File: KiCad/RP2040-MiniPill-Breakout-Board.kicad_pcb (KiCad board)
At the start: 2 copper layers, 56 x 72 mm, 8 parts, among them J1 Conn_01x20_Socket, J2 Conn_01x20_Socket, J3 Screw_Terminal_01x20, J4 Screw_Terminal_01x20

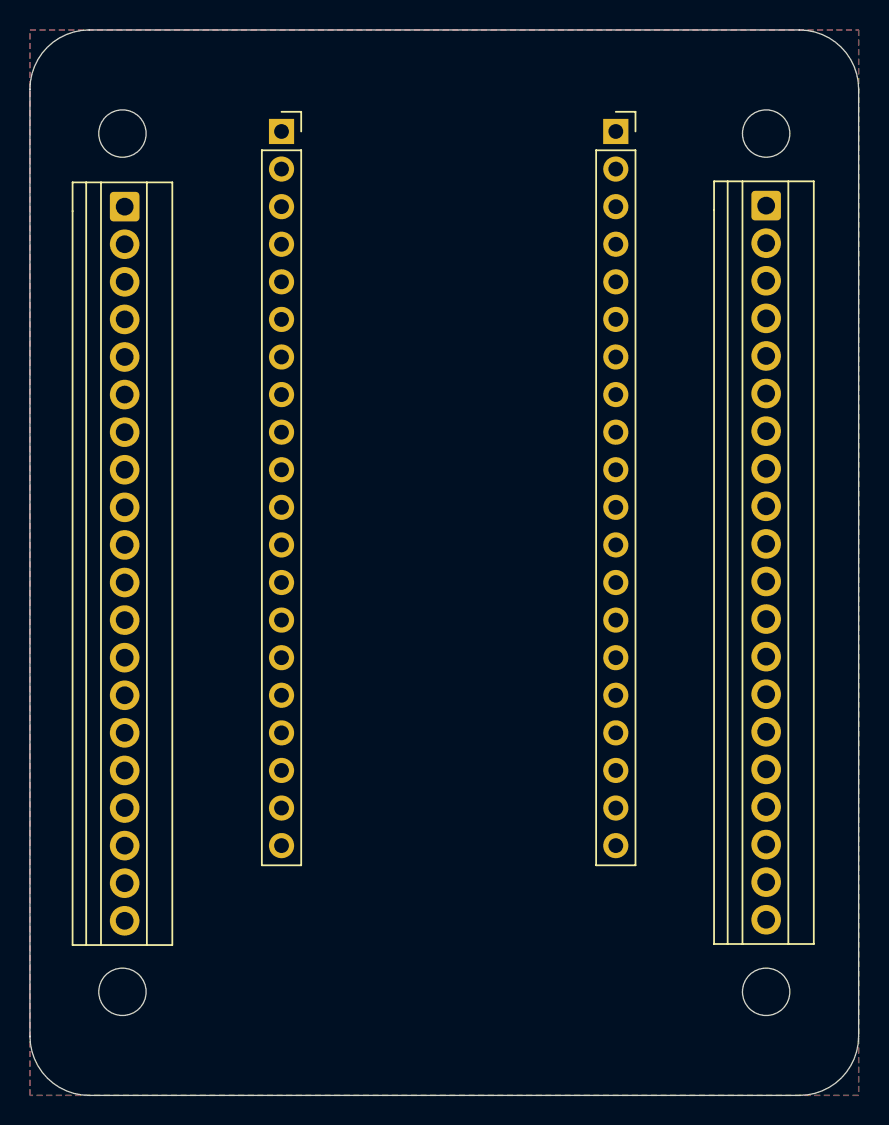
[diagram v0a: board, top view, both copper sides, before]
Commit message: adding Batteryholder
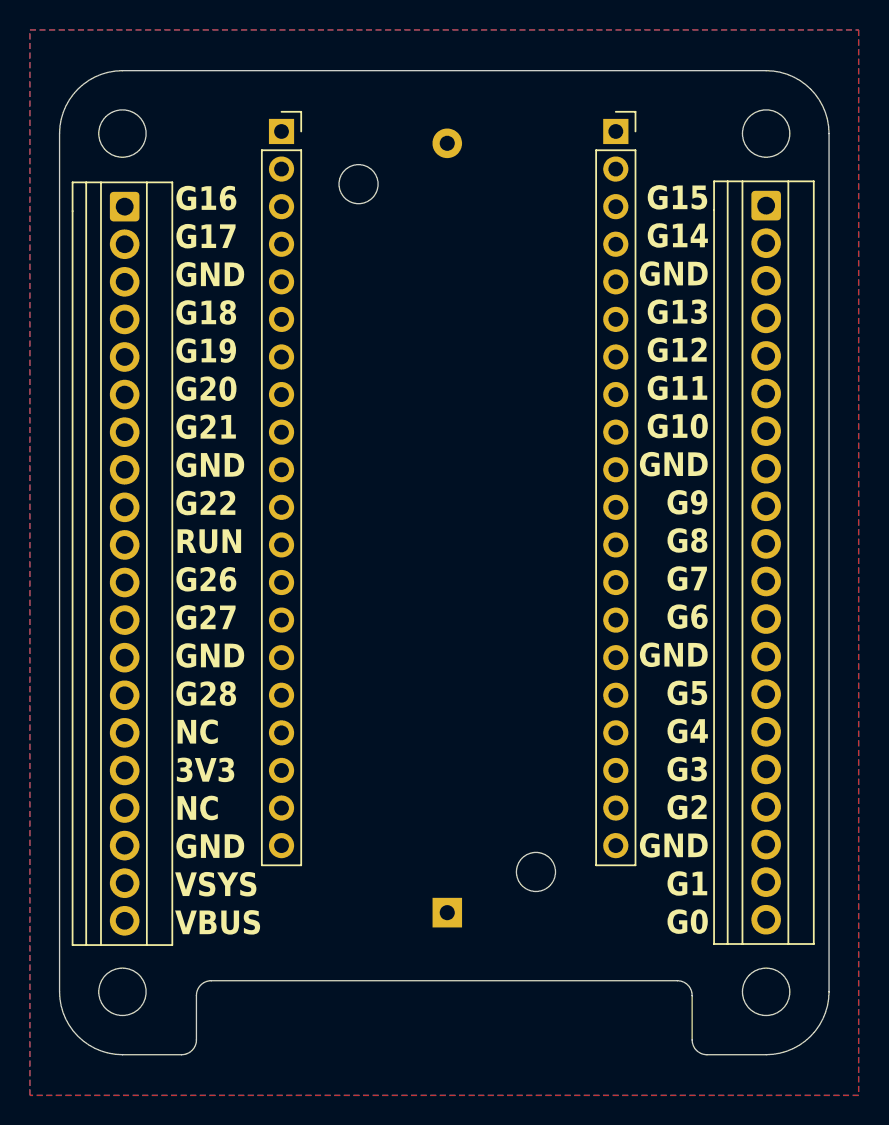
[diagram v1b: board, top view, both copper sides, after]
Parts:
- added BT1: Battery_Cell, Battery:BatteryHolder_Keystone_2460_1xAA, B.Cu at (144.4, 118.3)
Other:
- board size 56 x 72 mm -> 52 x 66.5 mm
- board text added: "G15 G14 GND G13 G12 G11 G10 GND G9 G8 G7 G6 GND G5 G4 G3 G2 GND G1 G0"
- board text added: "G16 G17 GND G18 G19 G20 G21 GND G22 RUN G26 G27 GND G28 NC 3V3 NC GND VSYS VBUS"

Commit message: Making some finetuning of 3dmodels. Adding aimation to README file.
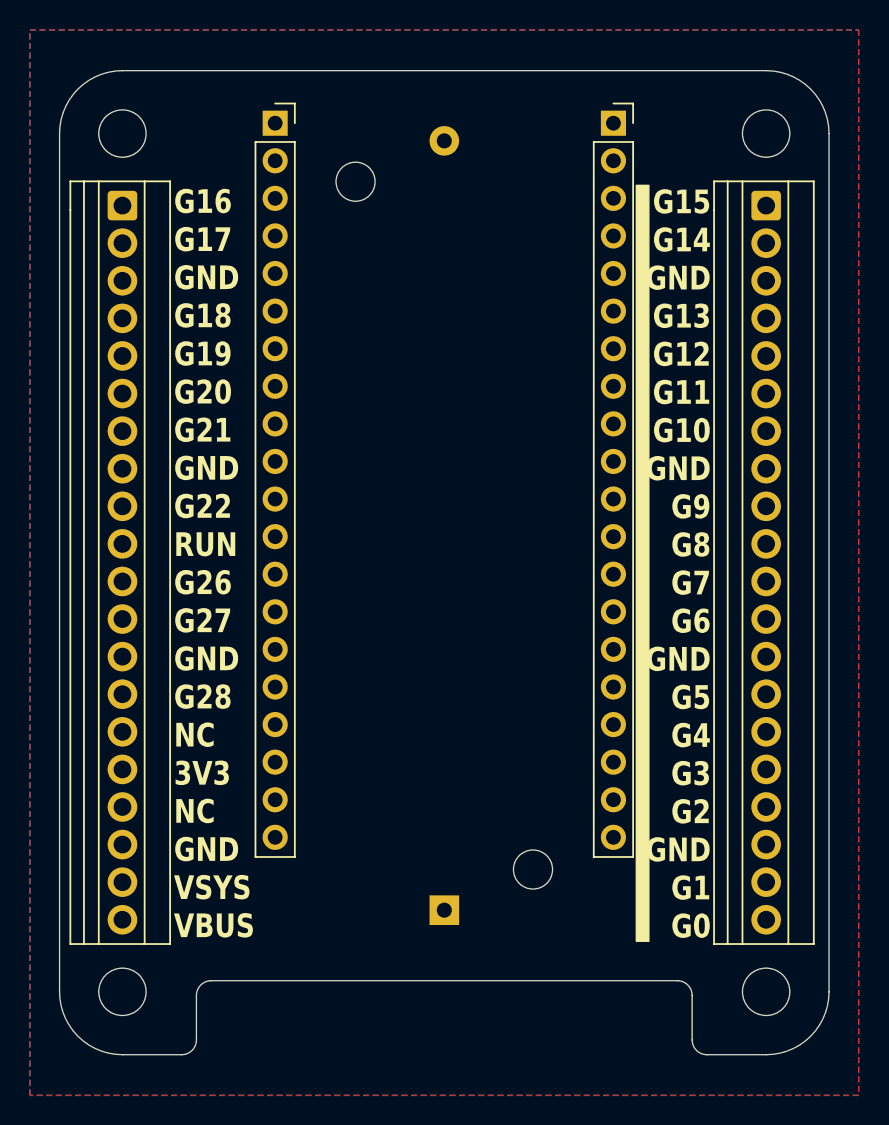
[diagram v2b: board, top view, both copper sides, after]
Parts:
- moved J1 0.71 mm to (132.8, 65.0)
- moved J2 0.58 mm to (155.6, 65.0)
- moved BT1 0.26 mm to (144.2, 118.2)
- moved J3 0.17 mm to (122.5, 70.6)
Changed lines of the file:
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@@
 	(net 82 "unconnected-(BT1---Pad2)")
 	(footprint "TerminalBlock:TerminalBlock_Xinya_XY308-2.54-20P_1x20_P2.54mm_Horizontal"
+		(locked yes)
 		(layer "F.Cu")
-		(at 122.6 70.64 -90)
+		(at 122.45 70.57 -90)
 		(descr "Terminal Block Xinya XY308-2.54-20P, 20 pins, pitch 2.54mm, size 51.3x6.5mm, drill diameter 1.2mm, pad diameter 2mm, http://www.xinyaelectronic.com/product/xy308-254, script-generated using https://gitlab.com/kicad/libraries/kicad-footprint-generator/-/tree/master/scripts/TerminalBlock_Xinya")
 		(tags "THT Terminal Block Xinya XY308-2.54-20P pitch 2.54mm size 51.3x6.5mm drill 1.2mm pad 2mm")
@@
 		(model "${KIPRJMOD}/Libraries/3dmodels/pxc_1725737_09_02_MPT-0-5-10-2-54_3D.stp"
 			(offset
-				(xyz -1.27 -3.175 0)
+				(xyz -1.4478 -3.048 0)
 			)
 			(scale
@@
 		(model "${KIPRJMOD}/Libraries/3dmodels/pxc_1725737_09_02_MPT-0-5-10-2-54_3D.stp"
 			(offset
-				(xyz 24.13 -3.175 0)
+				(xyz 23.9268 -3.048 0)
 			)
 			(scale
@@
 	)
 	(footprint "TerminalBlock:TerminalBlock_Xinya_XY308-2.54-20P_1x20_P2.54mm_Horizontal"
+		(locked yes)
 		(layer "F.Cu")
 		(at 165.95 70.57 -90)
@@
 		)
 		(fp_text user "${REFERENCE}"
-			(at 24.13 2.15 90)
+			(at 0.005 -2.35 0)
 			(layer "F.Fab")
 			(effects
@@
 		(locked yes)
 		(layer "F.Cu")
-		(at 155.79 65.56)
+		(at 155.63 65)
 		(descr "Through hole straight socket strip, 1x20, 2.54mm pitch, single row (from Kicad 4.0.7), script generated")
 		(tags "Through hole socket strip THT 1x20 2.54mm single row")
@@
 		(embedded_fonts no)
 		(model "${KIPRJMOD}/Libraries/3dmodels/5U210010_PC 210010 G 5U.stp"
+			(hide yes)
 			(opacity 0.4300)
 			(offset
@@
 		(locked yes)
 		(layer "F.Cu")
-		(at 133.2 65.56)
+		(at 132.77 65)
 		(descr "Through hole straight socket strip, 1x20, 2.54mm pitch, single row (from Kicad 4.0.7), script generated")
 		(tags "Through hole socket strip THT 1x20 2.54mm single row")
@@
 	)
 	(footprint "Battery:BatteryHolder_Keystone_2460_1xAA"
+		(locked yes)
 		(layer "B.Cu")
-		(at 144.4 118.35 90)
+		(at 144.2 118.185 90)
 		(descr "https://www.keyelco.com/product-pdf.cfm?p=1025")
 		(tags "AA battery cell holder")
@@
 			(at -0.02 9.42 90)
 			(layer "B.SilkS")
+			(hide yes)
 			(effects
 				(font
@@
 			(at 24.5 0 90)
 			(layer "B.Fab")
+			(hide yes)
 			(effects
 				(font
@@
 			)
 		)
-		(model "${KIPRJMOD}/Libraries/3dmodels/2460.STEP"
+		(model "${KIPRJMOD}/Libraries/3dmodels/2460_shorted.STEP"
 			(offset
-				(xyz 23 0.75 10.5)
+				(xyz 23 0.7499999986 10.16980001)
 			)
 			(scale
@@
 		)
 	)
+	(gr_rect
+		(start 157.175 69.2)
+		(end 158.025 120.285)
+		(stroke
+			(width 0.09)
+			(type solid)
+		)
+		(fill yes)
+		(locked yes)
+		(layer "F.SilkS")
+	)
 	(gr_line
 		(start 122.45 61.45)
@@
 	)
 	(gr_text "G16\nG17\nGND\nG18\nG19\nG20\nG21\nGND\nG22\nRUN\nG26\nG27\nGND\nG28\nNC\n3V3\nNC\nGND\nVSYS\nVBUS"
-		(at 126 120 0)
+		(locked yes)
+		(at 125.925 120.2 0)
 		(layer "F.SilkS" knockout)
 		(effects
 			(font
-				(size 1.6 1.4)
-				(thickness 0.25)
+				(size 1.6 1.3)
+				(thickness 0.275)
 				(bold yes)
 			)
@@
 	)
 	(gr_text "G15\nG14\nGND\nG13\nG12\nG11\nG10\nGND\nG9\nG8\nG7\nG6\nGND\nG5\nG4\nG3\nG2\nGND\nG1\nG0"
-		(at 162.1 119.95 0)
+		(locked yes)
+		(at 162.225 120.225 0)
 		(layer "F.SilkS" knockout)
 		(effects
 			(font
-				(size 1.6 1.4)
-				(thickness 0.25)
+				(size 1.6 1.3)
+				(thickness 0.275)
 				(bold yes)
 			)
@@
 			(keep_text_aligned yes)
 		)
-		(gr_text "56"
+		(gr_text "2204.7244"
 			(at 144.2 141.15 0)
 			(layer "Cmts.User")
@@
 		(layer "Cmts.User")
 		(pts
+			(xy 144.2 66.2) (xy 144.2 61.45)
+		)
+		(height -5.5)
+		(orientation 1)
+		(format
+			(prefix "")
+			(suffix "")
+			(units 3)
+			(units_format 0)
+			(precision 4)
+			(suppress_zeroes yes)
+		)
+		(style
+			(thickness 0.1)
+			(arrow_length 1.27)
+			(text_position_mode 0)
+			(arrow_direction outward)
+			(extension_height 0.58642)
+			(extension_offset 0.5)
+			(keep_text_aligned yes)
+		)
+		(gr_text "187.0079"
+			(at 137.55 63.825 90)
+			(layer "Cmts.User")
+			(effects
+				(font
+					(size 1 1)
+					(thickness 0.15)
+				)
+			)
+		)
+	)
+	(dimension
+		(type orthogonal)
+		(layer "Cmts.User")
+		(pts
 			(xy 122.45 65.7) (xy 165.95 65.7)
 		)
@@
 			(keep_text_aligned yes)
 		)
-		(gr_text "43.5"
+		(gr_text "1712.5984"
 			(at 144.2 135.65 0)
 			(layer "Cmts.User")
@@
 			(keep_text_aligned yes)
 		)
-		(gr_text "58"
+		(gr_text "2283.4646"
 			(at 178.05 94.7 90)
 			(layer "Cmts.User")
@@
 			(keep_text_aligned yes)
 		)
-		(gr_text "72"
+		(gr_text "2834.6457"
 			(at 185.15 94.7 90)
 			(layer "Cmts.User")
 			(effects
+				(font
+					(size 1 1)
+					(thickness 0.15)
+				)
+			)
+		)
+	)
+	(dimension
+		(type orthogonal)
+		(layer "Cmts.User")
+		(pts
+			(xy 144.2 118.185) (xy 144.2 122.95)
+		)
+		(height -4.5)
+		(orientation 1)
+		(format
+			(prefix "")
+			(suffix "")
+			(units 3)
+			(units_format 0)
+			(precision 4)
+			(suppress_zeroes yes)
+		)
+		(style
+			(thickness 0.1)
+			(arrow_length 1.27)
+			(text_position_mode 0)
+			(arrow_direction outward)
+			(extension_height 0.58642)
+			(extension_offset 0.5)
+			(keep_text_aligned yes)
+		)
+		(gr_text "187.5984"
+			(at 138.55 120.5675 90)
+			(layer "Cmts.User")
+			(effects
+				(font
+					(size 1 1)
+					(thickness 0.15)
+				)
+			)
+		)
+	)
+	(dimension
+		(type orthogonal)
+		(layer "Cmts.User")
+		(pts
+			(xy 132.77 65) (xy 155.63 65)
+		)
+		(height -9.75)
+		(orientation 0)
+		(format
+			(prefix "")
+			(suffix "")
+			(units 3)
+			(units_format 0)
+			(precision 4)
+			(suppress_zeroes yes)
+		)
+		(style
+			(thickness 0.1)
+			(arrow_length 1.27)
+			(text_position_mode 0)
+			(arrow_direction outward)
+			(extension_height 0.58642)
+			(extension_offset 0.5)
+			(keep_text_aligned yes)
+		)
+		(gr_text "900"
+			(at 144.2 54.1 0)
+			(layer "Cmts.User")
+			(effects

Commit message: adding over and undervoltage monitoring
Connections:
- J1 pad 1: unconnected-(J1-Pin_1-Pad1) -> Net-(J1-Pin_1)
- J1 pad 10: unconnected-(J1-Pin_10-Pad10) -> Net-(J1-Pin_10)
- J1 pad 11: unconnected-(J1-Pin_11-Pad11) -> Net-(J1-Pin_11)
- J1 pad 12: unconnected-(J1-Pin_12-Pad12) -> Net-(J1-Pin_12)
- J1 pad 13: unconnected-(J1-Pin_13-Pad13) -> /GND
- J1 pad 14: unconnected-(J1-Pin_14-Pad14) -> Net-(J1-Pin_14)
- J1 pad 15: unconnected-(J1-Pin_15-Pad15) -> Net-(J1-Pin_15)
- J1 pad 16: unconnected-(J1-Pin_16-Pad16) -> Net-(J1-Pin_16)
- J1 pad 17: unconnected-(J1-Pin_17-Pad17) -> Net-(J1-Pin_17)
- J1 pad 18: unconnected-(J1-Pin_18-Pad18) -> /GND
- J1 pad 19: unconnected-(J1-Pin_19-Pad19) -> Net-(J1-Pin_19)
- J1 pad 2: unconnected-(J1-Pin_2-Pad2) -> Net-(J1-Pin_2)
- J1 pad 20: unconnected-(J1-Pin_20-Pad20) -> Net-(J1-Pin_20)
- J1 pad 3: unconnected-(J1-Pin_3-Pad3) -> /GND
- J1 pad 4: unconnected-(J1-Pin_4-Pad4) -> Net-(J1-Pin_4)
- J1 pad 5: unconnected-(J1-Pin_5-Pad5) -> Net-(J1-Pin_5)
- J1 pad 6: unconnected-(J1-Pin_6-Pad6) -> Net-(J1-Pin_6)
- J1 pad 7: unconnected-(J1-Pin_7-Pad7) -> Net-(J1-Pin_7)
- J1 pad 8: unconnected-(J1-Pin_8-Pad8) -> /GND
- J1 pad 9: unconnected-(J1-Pin_9-Pad9) -> Net-(J1-Pin_9)
- J2 pad 1: unconnected-(J2-Pin_1-Pad1) -> Net-(J2-Pin_1)
- J2 pad 10: unconnected-(J2-Pin_10-Pad10) -> Net-(J2-Pin_10)
- J2 pad 11: unconnected-(J2-Pin_11-Pad11) -> Net-(J2-Pin_11)
- J2 pad 12: unconnected-(J2-Pin_12-Pad12) -> Net-(J2-Pin_12)
- J2 pad 13: unconnected-(J2-Pin_13-Pad13) -> /GND
- J2 pad 14: unconnected-(J2-Pin_14-Pad14) -> Net-(J2-Pin_14)
- J2 pad 15: unconnected-(J2-Pin_15-Pad15) -> Net-(J2-Pin_15)
- J2 pad 16: unconnected-(J2-Pin_16-Pad16) -> Net-(J2-Pin_16)
- J2 pad 17: unconnected-(J2-Pin_17-Pad17) -> Net-(J2-Pin_17)
- J2 pad 18: unconnected-(J2-Pin_18-Pad18) -> /GND
- J2 pad 19: unconnected-(J2-Pin_19-Pad19) -> Net-(J2-Pin_19)
- J2 pad 2: unconnected-(J2-Pin_2-Pad2) -> Net-(J2-Pin_2)
- J2 pad 20: unconnected-(J2-Pin_20-Pad20) -> Net-(J2-Pin_20)
- J2 pad 3: unconnected-(J2-Pin_3-Pad3) -> /GND
- J2 pad 4: unconnected-(J2-Pin_4-Pad4) -> Net-(J2-Pin_4)
- J2 pad 5: unconnected-(J2-Pin_5-Pad5) -> Net-(J2-Pin_5)
- J2 pad 6: unconnected-(J2-Pin_6-Pad6) -> Net-(J2-Pin_6)
- J2 pad 7: unconnected-(J2-Pin_7-Pad7) -> Net-(J2-Pin_7)
- J2 pad 8: unconnected-(J2-Pin_8-Pad8) -> /GND
- J2 pad 9: unconnected-(J2-Pin_9-Pad9) -> Net-(J2-Pin_9)
- J3 pad 1: unconnected-(J3-Pin_1-Pad1) -> Net-(J1-Pin_1)
- J3 pad 10: unconnected-(J3-Pin_10-Pad10) -> Net-(J1-Pin_10)
- J3 pad 11: unconnected-(J3-Pin_11-Pad11) -> Net-(J1-Pin_11)
- J3 pad 12: unconnected-(J3-Pin_12-Pad12) -> Net-(J1-Pin_12)
- J3 pad 13: unconnected-(J3-Pin_13-Pad13) -> /GND
- J3 pad 14: unconnected-(J3-Pin_14-Pad14) -> Net-(J1-Pin_14)
- J3 pad 15: unconnected-(J3-Pin_15-Pad15) -> Net-(J1-Pin_15)
- J3 pad 16: unconnected-(J3-Pin_16-Pad16) -> Net-(J1-Pin_16)
- J3 pad 17: unconnected-(J3-Pin_17-Pad17) -> Net-(J1-Pin_17)
- J3 pad 18: unconnected-(J3-Pin_18-Pad18) -> /GND
- J3 pad 19: unconnected-(J3-Pin_19-Pad19) -> Net-(J1-Pin_19)
- J3 pad 2: unconnected-(J3-Pin_2-Pad2) -> Net-(J1-Pin_2)
- J3 pad 20: unconnected-(J3-Pin_20-Pad20) -> Net-(J1-Pin_20)
- J3 pad 3: unconnected-(J3-Pin_3-Pad3) -> /GND
- J3 pad 4: unconnected-(J3-Pin_4-Pad4) -> Net-(J1-Pin_4)
- J3 pad 5: unconnected-(J3-Pin_5-Pad5) -> Net-(J1-Pin_5)
- J3 pad 6: unconnected-(J3-Pin_6-Pad6) -> Net-(J1-Pin_6)
- J3 pad 7: unconnected-(J3-Pin_7-Pad7) -> Net-(J1-Pin_7)
- J3 pad 8: unconnected-(J3-Pin_8-Pad8) -> /GND
- J3 pad 9: unconnected-(J3-Pin_9-Pad9) -> Net-(J1-Pin_9)
- J4 pad 1: unconnected-(J4-Pin_1-Pad1) -> Net-(J2-Pin_1)
- J4 pad 10: unconnected-(J4-Pin_10-Pad10) -> Net-(J2-Pin_10)
- J4 pad 11: unconnected-(J4-Pin_11-Pad11) -> Net-(J2-Pin_11)
- J4 pad 12: unconnected-(J4-Pin_12-Pad12) -> Net-(J2-Pin_12)
- J4 pad 13: unconnected-(J4-Pin_13-Pad13) -> /GND
- J4 pad 14: unconnected-(J4-Pin_14-Pad14) -> Net-(J2-Pin_14)
- J4 pad 15: unconnected-(J4-Pin_15-Pad15) -> Net-(J2-Pin_15)
- J4 pad 16: unconnected-(J4-Pin_16-Pad16) -> Net-(J2-Pin_16)
- J4 pad 17: unconnected-(J4-Pin_17-Pad17) -> Net-(J2-Pin_17)
- J4 pad 18: unconnected-(J4-Pin_18-Pad18) -> /GND
- J4 pad 19: unconnected-(J4-Pin_19-Pad19) -> Net-(J2-Pin_19)
- J4 pad 2: unconnected-(J4-Pin_2-Pad2) -> Net-(J2-Pin_2)
- J4 pad 20: unconnected-(J4-Pin_20-Pad20) -> Net-(J2-Pin_20)
- J4 pad 3: unconnected-(J4-Pin_3-Pad3) -> /GND
- J4 pad 4: unconnected-(J4-Pin_4-Pad4) -> Net-(J2-Pin_4)
- J4 pad 5: unconnected-(J4-Pin_5-Pad5) -> Net-(J2-Pin_5)
- J4 pad 6: unconnected-(J4-Pin_6-Pad6) -> Net-(J2-Pin_6)
- J4 pad 7: unconnected-(J4-Pin_7-Pad7) -> Net-(J2-Pin_7)
- J4 pad 8: unconnected-(J4-Pin_8-Pad8) -> /GND
- J4 pad 9: unconnected-(J4-Pin_9-Pad9) -> Net-(J2-Pin_9)
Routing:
- net Net-(J2-Pin_9): track 0.00 -> 12.6 mm
- net Net-(J2-Pin_7): track 0.00 -> 12.6 mm
- net Net-(J2-Pin_5): track 0.00 -> 12.6 mm
- net Net-(J2-Pin_12): track 0.00 -> 12.6 mm
- net Net-(J2-Pin_10): track 0.00 -> 12.6 mm
- net /GND: track 0.00 -> 12.6 mm
- net Net-(J2-Pin_6): track 0.00 -> 12.6 mm
- net Net-(J2-Pin_4): track 0.00 -> 12.6 mm
- net Net-(J2-Pin_2): track 0.00 -> 12.6 mm
- net Net-(J2-Pin_11): track 0.00 -> 12.6 mm
- net Net-(J2-Pin_1): track 0.00 -> 12.6 mm
- added copper zone on B.Cu, net /GND
- added copper zone on F.Cu, net /GND
- removed copper zone on B.Cu, net (none)
- removed copper zone on F.Cu, net (none)

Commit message: adding Simulation
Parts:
- added C1: C, Capacitor_SMD:C_0603_1608Metric_Pad1.08x0.95mm_HandSolder, F.Cu at (138.2, 106.2)
- added R1: 2K, Resistor_SMD:R_0603_1608Metric_Pad0.98x0.95mm_HandSolder, F.Cu at (141.3, 115.9)
- added R2: 100, Resistor_SMD:R_0603_1608Metric_Pad0.98x0.95mm_HandSolder, F.Cu at (137.2, 111.1)
- added R3: 220, Resistor_SMD:R_0603_1608Metric_Pad0.98x0.95mm_HandSolder, F.Cu at (138.8, 115.0)
- added R4: 50k, Resistor_SMD:R_0603_1608Metric_Pad0.98x0.95mm_HandSolder, F.Cu at (141.3, 114.1)
- added R5: 50k, Resistor_SMD:R_0603_1608Metric_Pad0.98x0.95mm_HandSolder, F.Cu at (138.2, 107.8)
- added R6: 50k, Resistor_SMD:R_0603_1608Metric_Pad0.98x0.95mm_HandSolder, F.Cu at (141.7, 107.8)
- added U1: TPS3700, Package_TO_SOT_SMD:SOT-23-6, F.Cu at (139.8, 111.1)
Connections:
- net Net-(J1-Pin_1) renamed /G16
- net Net-(J1-Pin_10) renamed /RUN
- net Net-(J1-Pin_11) renamed /G26
- net Net-(J1-Pin_12) renamed /G27
- net Net-(J1-Pin_14) renamed /G28
- net Net-(J1-Pin_16) renamed /3V3
- net Net-(J1-Pin_19) renamed /VSYS
- net Net-(J1-Pin_2) renamed /G17
- net Net-(J1-Pin_20) renamed /VBUS
- net Net-(J1-Pin_4) renamed /G18
- net Net-(J1-Pin_5) renamed /G19
- net Net-(J1-Pin_6) renamed /G20
- net Net-(J1-Pin_7) renamed /G21
- net Net-(J1-Pin_9) renamed /G22
- net Net-(J2-Pin_1) renamed /G15
- net Net-(J2-Pin_10) renamed /G8
- net Net-(J2-Pin_11) renamed /G7
- net Net-(J2-Pin_12) renamed /G6
- net Net-(J2-Pin_14) renamed /G5
- net Net-(J2-Pin_15) renamed /G4
- net Net-(J2-Pin_16) renamed /G3
- net Net-(J2-Pin_17) renamed /G2
- net Net-(J2-Pin_19) renamed /G1
- net Net-(J2-Pin_2) renamed /G14
- net Net-(J2-Pin_20) renamed /G0
- net Net-(J2-Pin_4) renamed /G13
- net Net-(J2-Pin_5) renamed /G12
- net Net-(J2-Pin_6) renamed /G11
- net Net-(J2-Pin_7) renamed /G10
- net Net-(J2-Pin_9) renamed /G9
- BT1 pad 1: unconnected-(BT1-+-Pad1) -> /VDD
- BT1 pad 2: unconnected-(BT1---Pad2) -> GND
- J1 pad 13: /GND -> GND
- J1 pad 15: Net-(J1-Pin_15) -> /NC
- J1 pad 17: Net-(J1-Pin_17) -> /NC
- J1 pad 18: /GND -> GND
- J1 pad 3: /GND -> GND
- J1 pad 8: /GND -> GND
- J2 pad 13: /GND -> GND
- J2 pad 18: /GND -> GND
- J2 pad 3: /GND -> GND
- J2 pad 8: /GND -> GND
- J3 pad 13: /GND -> GND
- J3 pad 15: Net-(J1-Pin_15) -> /NC
- J3 pad 17: Net-(J1-Pin_17) -> /NC
- J3 pad 18: /GND -> GND
- J3 pad 3: /GND -> GND
- J3 pad 8: /GND -> GND
- J4 pad 13: /GND -> GND
- J4 pad 18: /GND -> GND
- J4 pad 3: /GND -> GND
- J4 pad 8: /GND -> GND
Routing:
- net /NC: track 0.00 -> 25.3 mm
- net /G22: track 0.00 -> 12.6 mm
- net /RUN: track 0.00 -> 12.6 mm
- net /VBUS: track 0.00 -> 12.6 mm
- net /G5: track 0.00 -> 12.6 mm
- net /G28: track 0.00 -> 12.6 mm
- net /G21: track 0.00 -> 12.6 mm
- net /G19: track 0.00 -> 12.6 mm
- net /3V3: track 0.00 -> 12.6 mm
- net /VSYS: track 0.00 -> 12.6 mm
- net /G27: track 0.00 -> 12.6 mm
- net /G18: track 0.00 -> 12.6 mm
- net /G26: track 0.00 -> 12.6 mm
- net /G20: track 0.00 -> 12.6 mm
- net /G16: track 0.00 -> 12.6 mm
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- added copper zone on B.Cu, net GND
- added copper zone on F.Cu, net GND
- removed copper zone on B.Cu, net /GND
- removed copper zone on F.Cu, net /GND
